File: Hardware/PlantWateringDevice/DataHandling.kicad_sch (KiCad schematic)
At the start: 13 parts, among them J1 Conn_02x04_Counter_Clockwise, J5 Conn_02x03_Odd_Even, SW1 SW_DIP_x02, SW3 SW_Push, SW4 SW_DIP_x02, SW7 SW_DIP_x02, U4 PIC10F202-IOT

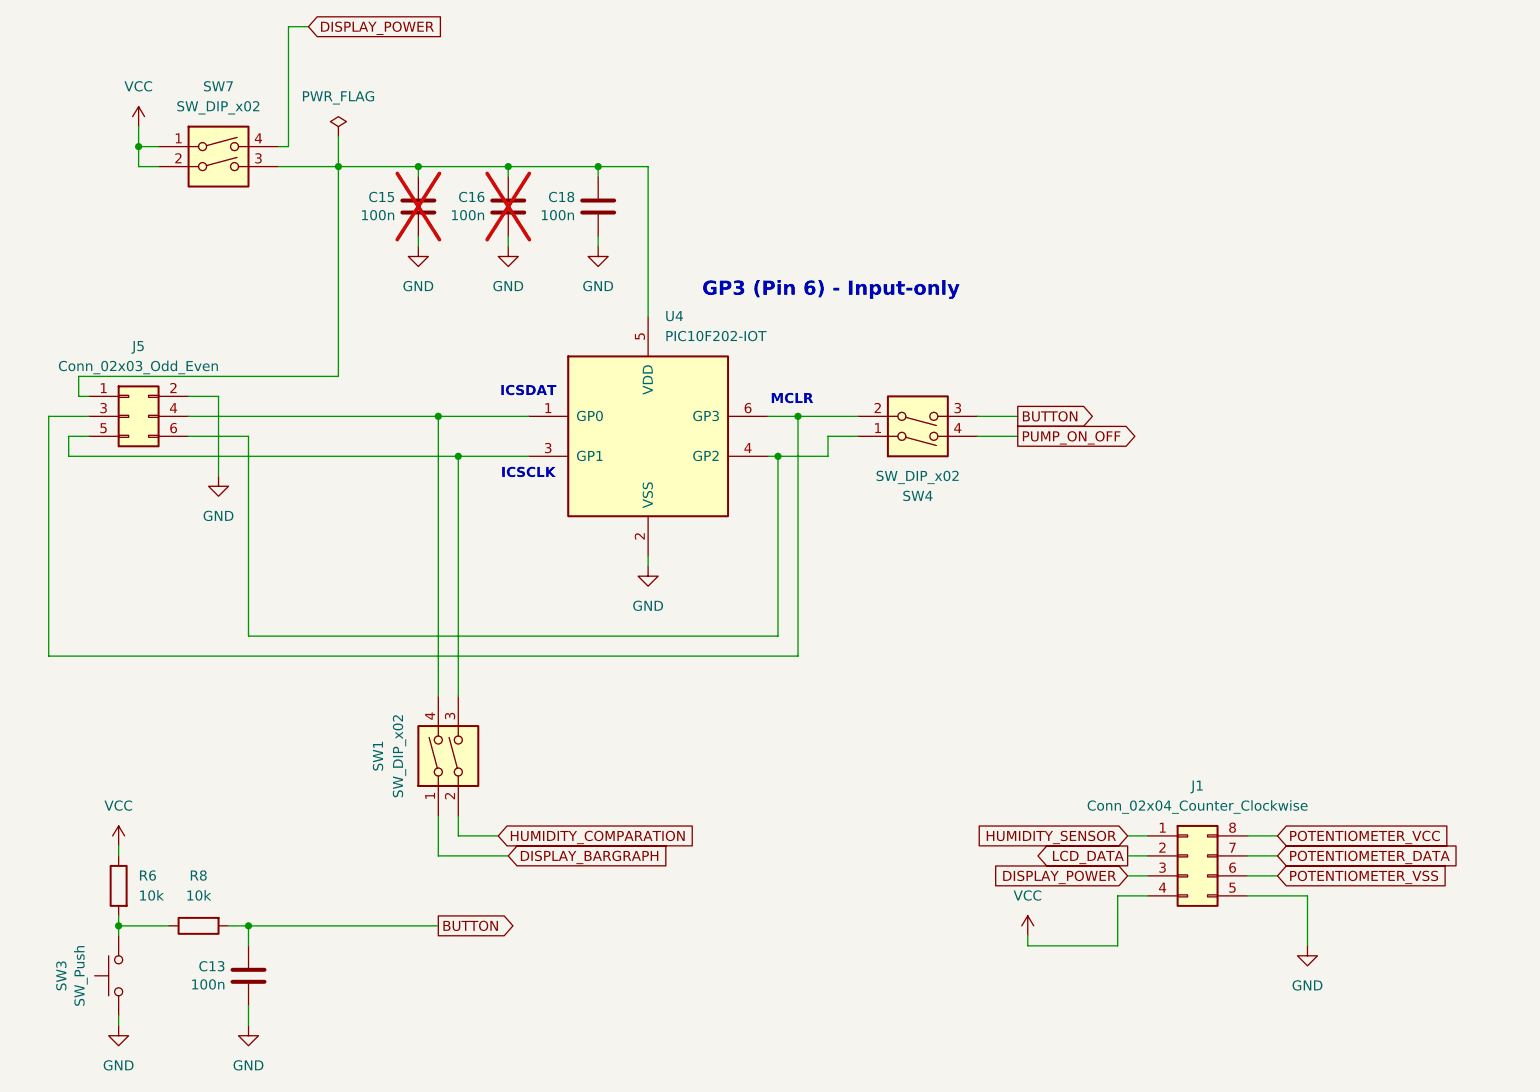
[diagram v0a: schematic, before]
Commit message: fix #16, fix #17, fix #18, fix #19, fix #20, fix #26, fix #27, fix #28, fix #30, fix #32, fix#33, fix #34, fix #35, fix #38
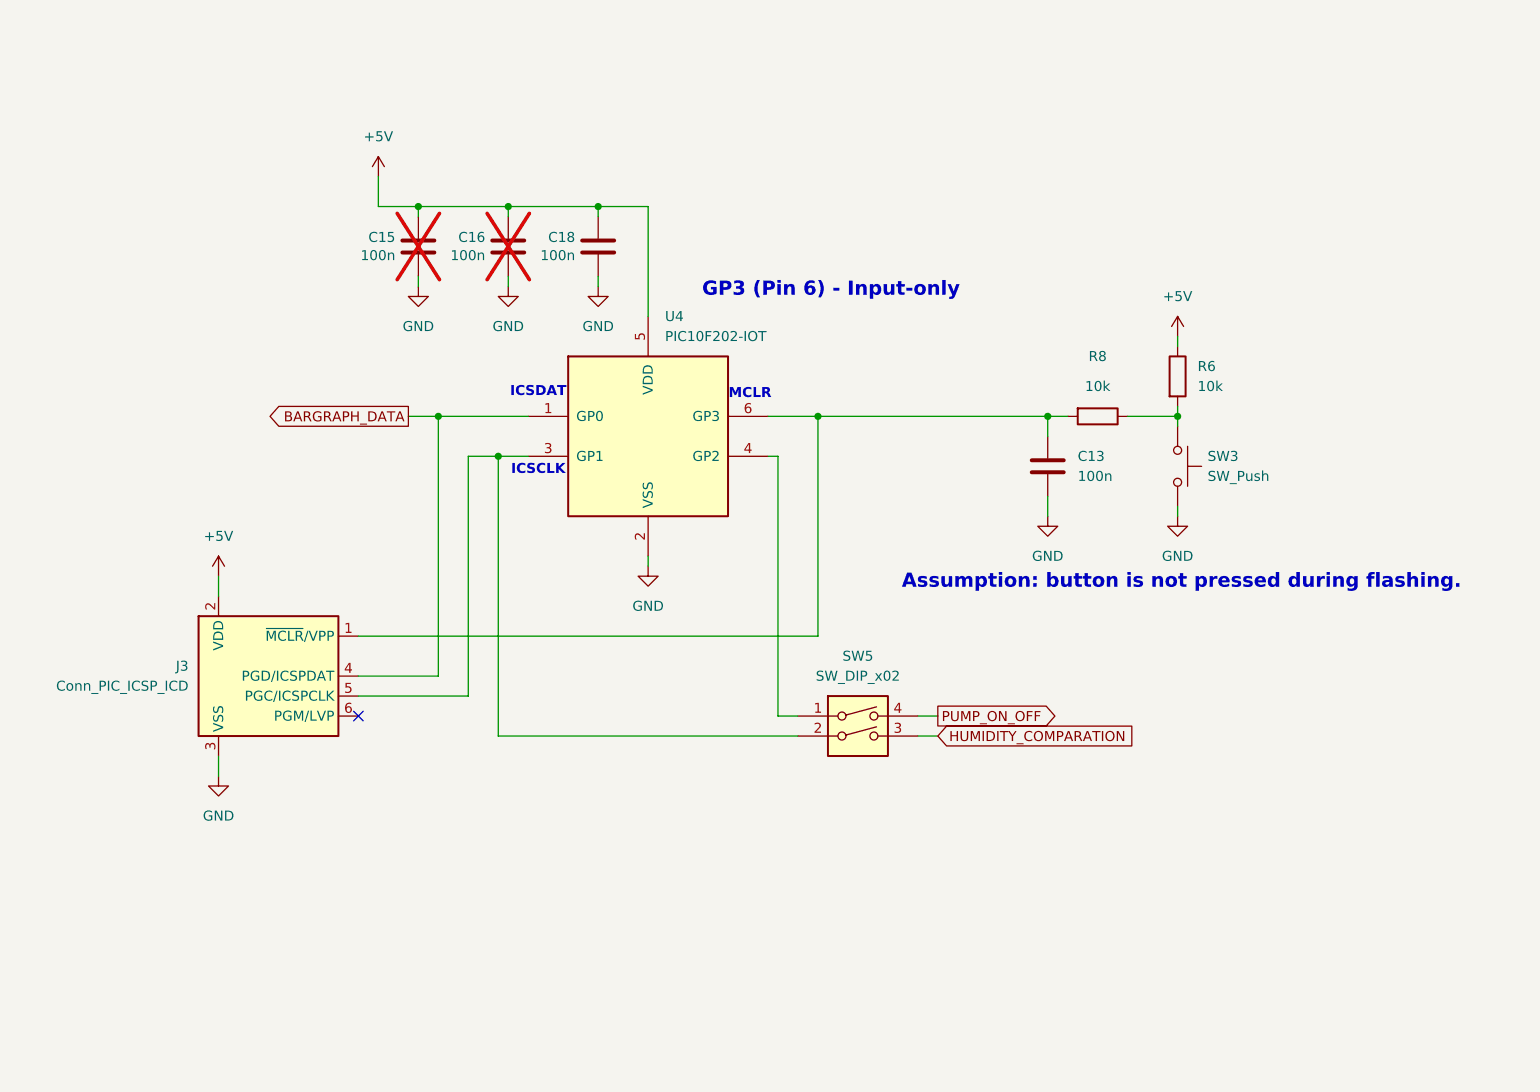
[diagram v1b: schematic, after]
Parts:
- removed J1: Conn_02x04_Counter_Clockwise, Connector_PinHeader_2.54mm:PinHeader_2x04_P2.54mm_Vertical, symbol Connector_Generic:Conn_02x04_Counter_Clockwise
- removed J5: Conn_02x03_Odd_Even, Connector_PinHeader_2.54mm:PinHeader_2x03_P2.54mm_Vertical, symbol Connector_Generic:Conn_02x03_Odd_Even
- removed SW1, SW4, SW7: SW_DIP_x02, Package_DIP:DIP-4_W7.62mm, symbol Switch:SW_DIP_x02
- added J3: Conn_PIC_ICSP_ICD, Connector_PinHeader_2.54mm:PinHeader_1x06_P2.54mm_Vertical, symbol Connector:Conn_PIC_ICSP_ICD
- added SW5: SW_DIP_x02, Package_DIP:DIP-4_W7.62mm, symbol Switch:SW_DIP_x02
- C13, C15, C16, C18: footprint Capacitor_SMD:C_0805_2012Metric -> Capacitor_SMD:C_0603_1608Metric
- R6, R8: footprint Resistor_SMD:R_0805_2012Metric -> Resistor_SMD:R_0603_1608Metric
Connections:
- net BUTTON is gone; now on an unnamed net: C13.1, R8.2
- net VCC is gone; now on net +5V: R6.1
- net GND: now also J3.3 (VSS)
- net HUMIDITY_COMPARATION: now also SW5.3
- net PUMP_ON_OFF: now also SW5.4
- net at U4.3 (GP1): now also J3.5 (PGC/ICSPCLK), SW5.2
- net BARGRAPH_DATA: now reaches U4.1 (GP0)
- net BARGRAPH_DATA: now also J3.4 (PGD/ICSPDAT)
- net +5V: now reaches C15.1, C16.1, C18.1, U4.5 (VDD)
- net +5V: now also J3.2 (VDD)
- net at U4.4 (GP2): now also SW5.1
- net at U4.6 (GP3): now also J3.1 (~{MCLR}/VPP)
- no-connect marks 0 -> 1
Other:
- note added: "Assumption: button is not pressed during flashing."
- moved on the sheet: C13, C15, C16, C18, R6, R8, SW3

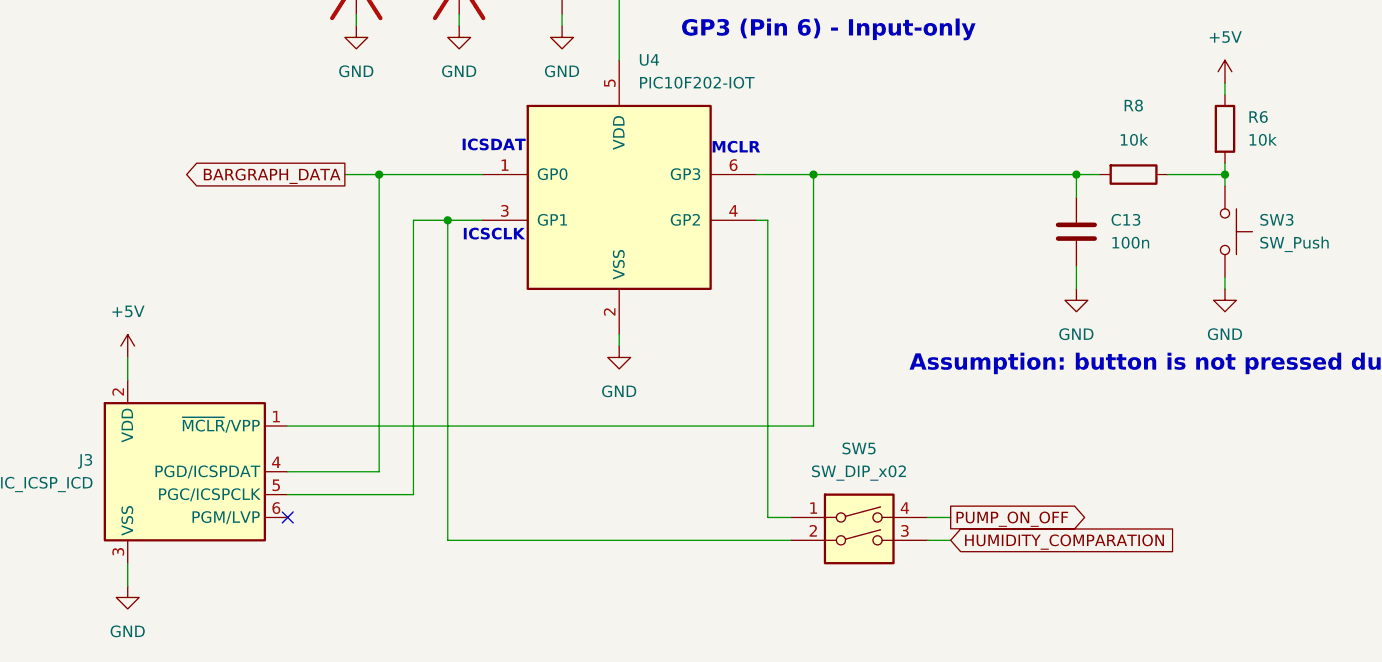
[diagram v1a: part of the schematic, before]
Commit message: hierarchical block diagram structure in kicad
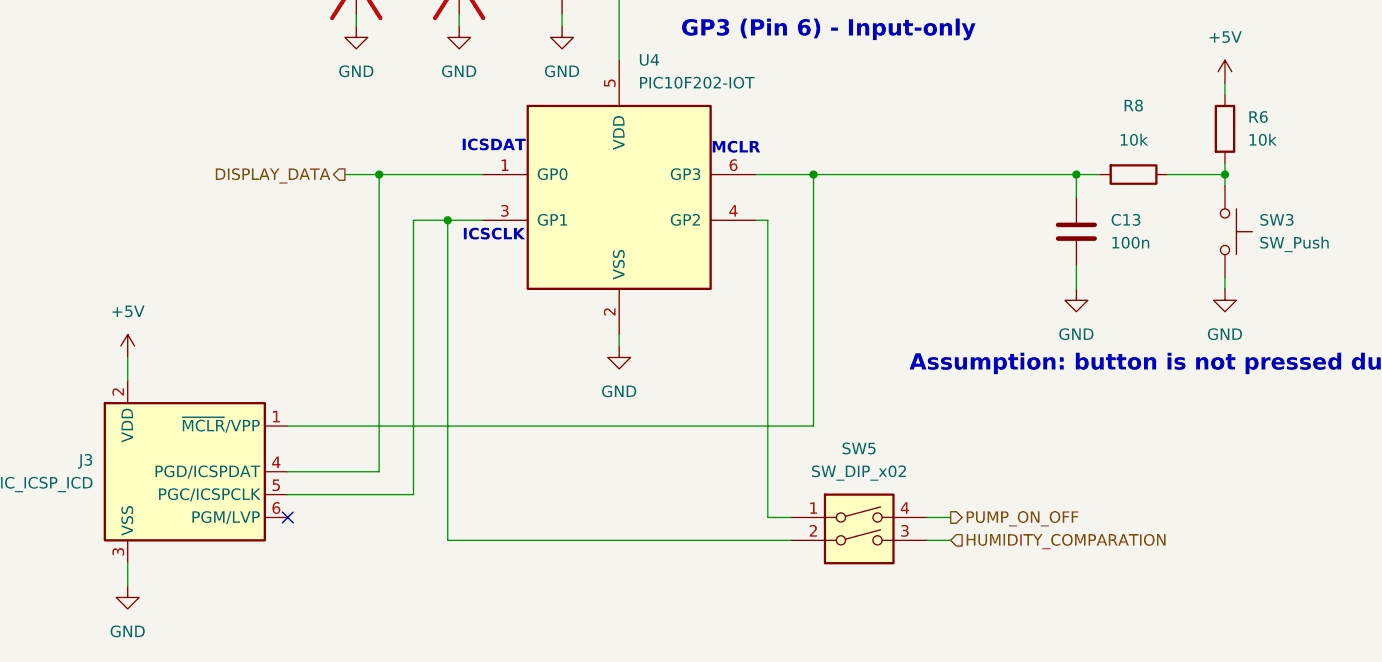
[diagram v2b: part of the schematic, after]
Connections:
- net BARGRAPH_DATA renamed DISPLAY_DATA
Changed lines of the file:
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@@
 (kicad_sch
-	(version 20260101)
+	(version 20260306)
 	(generator "eeschema")
 	(generator_version "10.0")
@@
 		)
 	)
-	(global_label "PUMP_ON_OFF"
+	(hierarchical_label "PUMP_ON_OFF"
 		(shape output)
 		(at 190.5 119.38 0)
-		(fields_autoplaced yes)
 		(effects
 			(font
@@
 			(justify left)
 		)
-		(property "Intersheetrefs" "${INTERSHEET_REFS}"
-			(at 206.911 119.38 0)
-			(hide yes)
-			(show_name no)
-			(do_not_autoplace no)
-			(effects
-				(font
-					(size 1.27 1.27)
-				)
-				(justify left)
-			)
-		)
-	)
-	(global_label "HUMIDITY_COMPARATION"
+	)
+	(hierarchical_label "HUMIDITY_COMPARATION"
 		(shape input)
 		(at 190.5 121.92 0)
-		(fields_autoplaced yes)
 		(effects
 			(font
@@
 			(justify left)
 		)
-		(property "Intersheetrefs" "${INTERSHEET_REFS}"
-			(at 216.1035 121.92 0)
-			(hide yes)
-			(show_name no)
-			(do_not_autoplace no)
-			(effects
-				(font
-					(size 1.27 1.27)
-				)
-				(justify left)
-			)
-		)
-	)
-	(global_label "BARGRAPH_DATA"
+	)
+	(hierarchical_label "DISPLAY_DATA"
 		(shape output)
 		(at 123.19 81.28 180)
-		(fields_autoplaced yes)
 		(effects
 			(font
@@
 			)
 			(justify right)
-		)
-		(property "Intersheetrefs" "${INTERSHEET_REFS}"
-			(at 104.9647 81.28 0)
-			(hide yes)
-			(show_name no)
-			(do_not_autoplace no)
-			(effects
-				(font
-					(size 1.27 1.27)
-				)
-				(justify right)
-			)
 		)
 	)
@@
 		)
 		(instances
-			(project ""
+			(project "PlantWateringDevice"
 				(path "/1ef241b3-83d7-48ae-bcca-b7d0eea44e63/774c5e66-df25-4246-b332-f6d1db12f11e"
 					(reference "J3")
@@
 		)
 		(instances
-			(project ""
+			(project "PlantWateringDevice"
 				(path "/1ef241b3-83d7-48ae-bcca-b7d0eea44e63/774c5e66-df25-4246-b332-f6d1db12f11e"
 					(reference "U4")
